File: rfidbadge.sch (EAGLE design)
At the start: 49 parts, among them Q1 BSS123, U1 ATMEGA328P_TQFP, U2 CLRC663, Y1 27.12 MHz

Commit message: Interrupted in the middle of starting the board
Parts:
- L1: value (none) -> 22 nH
- Q1: PROD_ID (none) -> 2N7002ET1GOSCT-ND
- U$1: PROD_ID (none) -> 36-2479-ND
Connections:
- new net N$10: C4.1, U2.AVDD
- new net N$11: C3.1, U2.DVDD
- net VDD: no longer C3.1, C4.1, U2.AVDD, U2.DVDD
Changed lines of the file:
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@@
 <attribute name="PROD_ID" value="311-1443-1-ND"/>
 </part>
-<part name="L1" library="rcl" deviceset="L-US" device="L0201"/>
+<part name="L1" library="rcl" deviceset="L-US" device="L0201" value="22 nH"/>
 <part name="C9" library="rcl" deviceset="C-EU" device="C0603K" value="0.1 uF">
 <attribute name="PROD_ID" value="311-1088-1-ND"/>
@@
 <part name="VDD4" library="supply1" deviceset="VDD" device=""/>
 <part name="R1" library="rcl" deviceset="R-US_" device="R0603" value="56"/>
-<part name="Q1" library="transistor-small-signal" deviceset="BSS123" device=""/>
+<part name="Q1" library="transistor-small-signal" deviceset="BSS123" device="">
+<attribute name="PROD_ID" value="2N7002ET1GOSCT-ND"/>
+</part>
 <part name="GND8" library="supply1" deviceset="GND" device=""/>
 <part name="ISP" library="pinhead" deviceset="PINHD-2X3" device=""/>
@@
 <attribute name="PROD_ID" value="311-1060-1-ND"/>
 </part>
-<part name="U$1" library="battery_holder" deviceset="AAA_X3" device=""/>
+<part name="U$1" library="battery_holder" deviceset="AAA_X3" device="">
+<attribute name="PROD_ID" value="36-2479-ND"/>
+</part>
 <part name="GND10" library="supply1" deviceset="GND" device=""/>
 <part name="VDD6" library="supply1" deviceset="VDD" device=""/>
@@
 <instance part="GND3" gate="1" x="127" y="-58.42"/>
 <instance part="VDD1" gate="G$1" x="-30.48" y="35.56"/>
-<instance part="VDD2" gate="G$1" x="45.72" y="-22.86"/>
+<instance part="VDD2" gate="G$1" x="43.18" y="-22.86"/>
 <instance part="C3" gate="G$1" x="66.04" y="-43.18">
 <attribute name="PROD_ID" x="66.04" y="-43.18" size="1.778" layer="96" display="off"/>
@@
 <instance part="VDD4" gate="G$1" x="-30.48" y="83.82"/>
 <instance part="R1" gate="G$1" x="-30.48" y="66.04" rot="R90"/>
-<instance part="Q1" gate="G$1" x="-30.48" y="53.34"/>
+<instance part="Q1" gate="G$1" x="-30.48" y="53.34">
+<attribute name="PROD_ID" x="-30.48" y="53.34" size="1.778" layer="96" display="off"/>
+</instance>
 <instance part="GND8" gate="1" x="-30.48" y="43.18"/>
 <instance part="ISP" gate="A" x="-15.24" y="-50.8"/>
@@
 <attribute name="PROD_ID" x="129.54" y="43.18" size="1.778" layer="96" display="off"/>
 </instance>
-<instance part="U$1" gate="G$1" x="91.44" y="76.2"/>
+<instance part="U$1" gate="G$1" x="91.44" y="76.2">
+<attribute name="PROD_ID" x="91.44" y="76.2" size="1.778" layer="96" display="off"/>
+</instance>
 <instance part="GND10" gate="1" x="91.44" y="66.04"/>
 <instance part="VDD6" gate="G$1" x="91.44" y="88.9"/>
@@
 </segment>
 <segment>
-<pinref part="VDD2" gate="G$1" pin="VDD"/>
-<wire x1="45.72" y1="-25.4" x2="45.72" y2="-27.94" width="0.1524" layer="91"/>
-<pinref part="U2" gate="G$1" pin="PVDD"/>
-<wire x1="45.72" y1="-27.94" x2="68.58" y2="-27.94" width="0.1524" layer="91"/>
-<pinref part="U2" gate="G$1" pin="VDD"/>
-<wire x1="68.58" y1="-30.48" x2="50.8" y2="-30.48" width="0.1524" layer="91"/>
-<wire x1="50.8" y1="-30.48" x2="45.72" y2="-30.48" width="0.1524" layer="91"/>
-<wire x1="45.72" y1="-30.48" x2="45.72" y2="-27.94" width="0.1524" layer="91"/>
-<junction x="45.72" y="-27.94"/>
-<pinref part="U2" gate="G$1" pin="AVDD"/>
-<wire x1="68.58" y1="-35.56" x2="58.42" y2="-35.56" width="0.1524" layer="91"/>
-<wire x1="58.42" y1="-35.56" x2="45.72" y2="-35.56" width="0.1524" layer="91"/>
-<wire x1="45.72" y1="-35.56" x2="45.72" y2="-30.48" width="0.1524" layer="91"/>
-<junction x="45.72" y="-30.48"/>
-<pinref part="U2" gate="G$1" pin="DVDD"/>
-<wire x1="68.58" y1="-38.1" x2="66.04" y2="-38.1" width="0.1524" layer="91"/>
-<wire x1="66.04" y1="-38.1" x2="45.72" y2="-38.1" width="0.1524" layer="91"/>
-<wire x1="45.72" y1="-38.1" x2="45.72" y2="-35.56" width="0.1524" layer="91"/>
-<junction x="45.72" y="-35.56"/>
-<pinref part="C3" gate="G$1" pin="1"/>
-<wire x1="66.04" y1="-40.64" x2="66.04" y2="-38.1" width="0.1524" layer="91"/>
-<junction x="66.04" y="-38.1"/>
-<pinref part="C4" gate="G$1" pin="1"/>
-<wire x1="58.42" y1="-40.64" x2="58.42" y2="-35.56" width="0.1524" layer="91"/>
-<junction x="58.42" y="-35.56"/>
-<pinref part="C5" gate="G$1" pin="1"/>
-<wire x1="50.8" y1="-40.64" x2="50.8" y2="-30.48" width="0.1524" layer="91"/>
-<junction x="50.8" y="-30.48"/>
-<pinref part="C6" gate="G$1" pin="1"/>
-<wire x1="43.18" y1="-40.64" x2="43.18" y2="-27.94" width="0.1524" layer="91"/>
-<wire x1="43.18" y1="-27.94" x2="45.72" y2="-27.94" width="0.1524" layer="91"/>
-</segment>
-<segment>
 <pinref part="C9" gate="G$1" pin="2"/>
 <wire x1="81.28" y1="58.42" x2="81.28" y2="55.88" width="0.1524" layer="91"/>
@@
 <pinref part="U$1" gate="G$1" pin="P$2"/>
 <wire x1="91.44" y1="86.36" x2="91.44" y2="83.82" width="0.1524" layer="91"/>
+</segment>
+<segment>
+<pinref part="U2" gate="G$1" pin="PVDD"/>
+<wire x1="43.18" y1="-27.94" x2="50.8" y2="-27.94" width="0.1524" layer="91"/>
+<pinref part="C6" gate="G$1" pin="1"/>
+<wire x1="50.8" y1="-27.94" x2="68.58" y2="-27.94" width="0.1524" layer="91"/>
+<wire x1="43.18" y1="-40.64" x2="43.18" y2="-27.94" width="0.1524" layer="91"/>
+<pinref part="VDD2" gate="G$1" pin="VDD"/>
+<wire x1="43.18" y1="-25.4" x2="43.18" y2="-27.94" width="0.1524" layer="91"/>
+<junction x="43.18" y="-27.94"/>
+<pinref part="U2" gate="G$1" pin="VDD"/>
+<wire x1="68.58" y1="-30.48" x2="50.8" y2="-30.48" width="0.1524" layer="91"/>
+<pinref part="C5" gate="G$1" pin="1"/>
+<wire x1="50.8" y1="-40.64" x2="50.8" y2="-30.48" width="0.1524" layer="91"/>
+<wire x1="50.8" y1="-30.48" x2="50.8" y2="-27.94" width="0.1524" layer="91"/>
+<junction x="50.8" y="-30.48"/>
+<junction x="50.8" y="-27.94"/>
 </segment>
 </net>
@@
 </segment>
 </net>
+<net name="N$10" class="0">
+<segment>
+<pinref part="U2" gate="G$1" pin="AVDD"/>
+<wire x1="68.58" y1="-35.56" x2="58.42" y2="-35.56" width="0.1524" layer="91"/>
+<pinref part="C4" gate="G$1" pin="1"/>
+<wire x1="58.42" y1="-40.64" x2="58.42" y2="-35.56" width="0.1524" layer="91"/>
+</segment>
+</net>
+<net name="N$11" class="0">
+<segment>
+<pinref part="U2" gate="G$1" pin="DVDD"/>
+<wire x1="68.58" y1="-38.1" x2="66.04" y2="-38.1" width="0.1524" layer="91"/>
+<pinref part="C3" gate="G$1" pin="1"/>
+<wire x1="66.04" y1="-40.64" x2="66.04" y2="-38.1" width="0.1524" layer="91"/>
+</segment>
+</net>

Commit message: Lots of layout
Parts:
- C10: device rcl:CPOL-US085CS-1AR -> SparkFun-Passives:CAP_POL7343; PROD_ID (none) -> 399-3772-1-ND
- C28: value (none) -> 0.1 uF; PROD_ID 311-1060-1-ND -> 311-1088-1-ND
- L1: device rcl:L-USL0201 -> SparkFun-Passives:INDUCTOR30OHM,1.8A; PROD_ID (none) -> 1276-6310-1-ND
- L2, L3: device rcl:L-USL0201 -> SparkFun-Passives:INDUCTOR30OHM,1.8A
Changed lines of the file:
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@@
 <attribute name="PROD_ID" value="311-1443-1-ND"/>
 </part>
-<part name="L1" library="rcl" deviceset="L-US" device="L0201" value="22 nH"/>
+<part name="L1" library="SparkFun-Passives" deviceset="INDUCTOR" device="30OHM,1.8A" value="22 nH">
+<attribute name="PROD_ID" value="1276-6310-1-ND"/>
+</part>
 <part name="C9" library="rcl" deviceset="C-EU" device="C0603K" value="0.1 uF">
 <attribute name="PROD_ID" value="311-1088-1-ND"/>
 </part>
-<part name="C10" library="rcl" deviceset="CPOL-US" device="085CS-1AR" value="100 uF"/>
+<part name="C10" library="SparkFun-Passives" deviceset="CAP_POL" device="7343" value="100 uF">
+<attribute name="PROD_ID" value="399-3772-1-ND"/>
+</part>
 <part name="LCD" library="display" deviceset="NHD-C12832A1Z" device=""/>
 <part name="GND6" library="supply1" deviceset="GND" device=""/>
@@
 <part name="R2" library="rcl" deviceset="R-US_" device="R0603" value="1K"/>
 <part name="R3" library="rcl" deviceset="R-US_" device="R0603" value="1K"/>
-<part name="L2" library="rcl" deviceset="L-US" device="L0201"/>
-<part name="L3" library="rcl" deviceset="L-US" device="L0201"/>
+<part name="L2" library="SparkFun-Passives" deviceset="INDUCTOR" device="30OHM,1.8A"/>
+<part name="L3" library="SparkFun-Passives" deviceset="INDUCTOR" device="30OHM,1.8A"/>
 <part name="C20" library="rcl" deviceset="C-EU" device="C0603K">
 <attribute name="PROD_ID" value="311-1060-1-ND"/>
@@
 <attribute name="PROD_ID" value="311-1060-1-ND"/>
 </part>
-<part name="C28" library="rcl" deviceset="C-EU" device="C0603K">
-<attribute name="PROD_ID" value="311-1060-1-ND"/>
+<part name="C28" library="rcl" deviceset="C-EU" device="C0603K" value="0.1 uF">
+<attribute name="PROD_ID" value="311-1088-1-ND"/>
 </part>
 <part name="U$1" library="battery_holder" deviceset="AAA_X3" device="">
@@
 <attribute name="PROD_ID" x="81.28" y="50.8" size="1.778" layer="96" rot="R180" display="off"/>
 </instance>
-<instance part="C10" gate="G$1" x="73.66" y="53.34" rot="MR0"/>
+<instance part="C10" gate="G$1" x="73.66" y="53.34" rot="MR0">
+<attribute name="PROD_ID" x="73.66" y="53.34" size="1.778" layer="96" rot="MR0" display="off"/>
+</instance>
 <instance part="LCD" gate="G$1" x="-15.24" y="68.58"/>
 <instance part="GND6" gate="1" x="27.94" y="53.34"/>

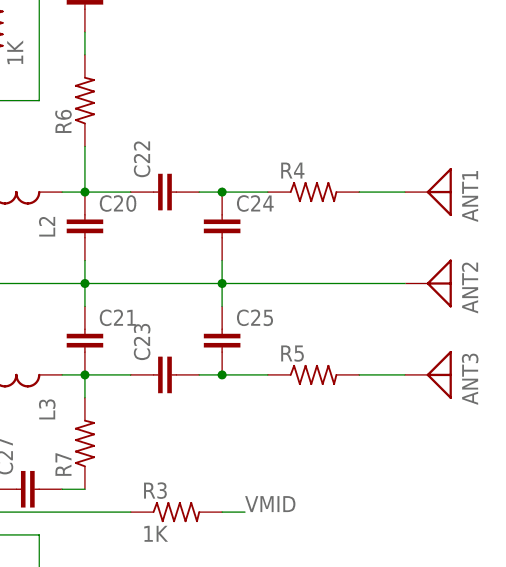
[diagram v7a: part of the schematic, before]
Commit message: Add antenna trace and ground planes
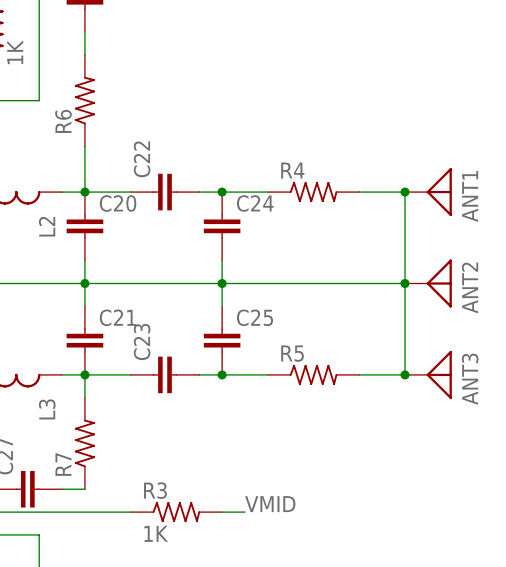
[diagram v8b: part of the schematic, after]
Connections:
- removed net N$5: ANT1.1, R4.2
- removed net N$6: ANT3.1, R5.2
- net GND: now also ANT1.1, ANT3.1, R4.2, R5.2
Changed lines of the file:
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@@
 <pinref part="ANT2" gate="A" pin="1"/>
 <wire x1="154.94" y1="0" x2="175.26" y2="0" width="0.1524" layer="91"/>
+<pinref part="R4" gate="G$1" pin="2"/>
+<pinref part="ANT1" gate="A" pin="1"/>
+<wire x1="170.18" y1="10.16" x2="175.26" y2="10.16" width="0.1524" layer="91"/>
+<wire x1="175.26" y1="10.16" x2="175.26" y2="0" width="0.1524" layer="91"/>
+<junction x="175.26" y="10.16"/>
+<junction x="175.26" y="0"/>
+<pinref part="R5" gate="G$1" pin="2"/>
+<pinref part="ANT3" gate="A" pin="1"/>
+<wire x1="170.18" y1="-10.16" x2="175.26" y2="-10.16" width="0.1524" layer="91"/>
+<wire x1="175.26" y1="0" x2="175.26" y2="-10.16" width="0.1524" layer="91"/>
+<junction x="175.26" y="-10.16"/>
 </segment>
 <segment>
@@
 </segment>
 </net>
-<net name="N$5" class="0">
-<segment>
-<pinref part="R4" gate="G$1" pin="2"/>
-<pinref part="ANT1" gate="A" pin="1"/>
-<wire x1="170.18" y1="10.16" x2="175.26" y2="10.16" width="0.1524" layer="91"/>
-</segment>
-</net>
-<net name="N$6" class="0">
-<segment>
-<pinref part="R5" gate="G$1" pin="2"/>
-<pinref part="ANT3" gate="A" pin="1"/>
-<wire x1="170.18" y1="-10.16" x2="175.26" y2="-10.16" width="0.1524" layer="91"/>
-</segment>
-</net>
